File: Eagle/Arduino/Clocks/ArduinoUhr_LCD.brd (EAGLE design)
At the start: 100 x 80 mm, 27 parts, among them IC1 UA748P

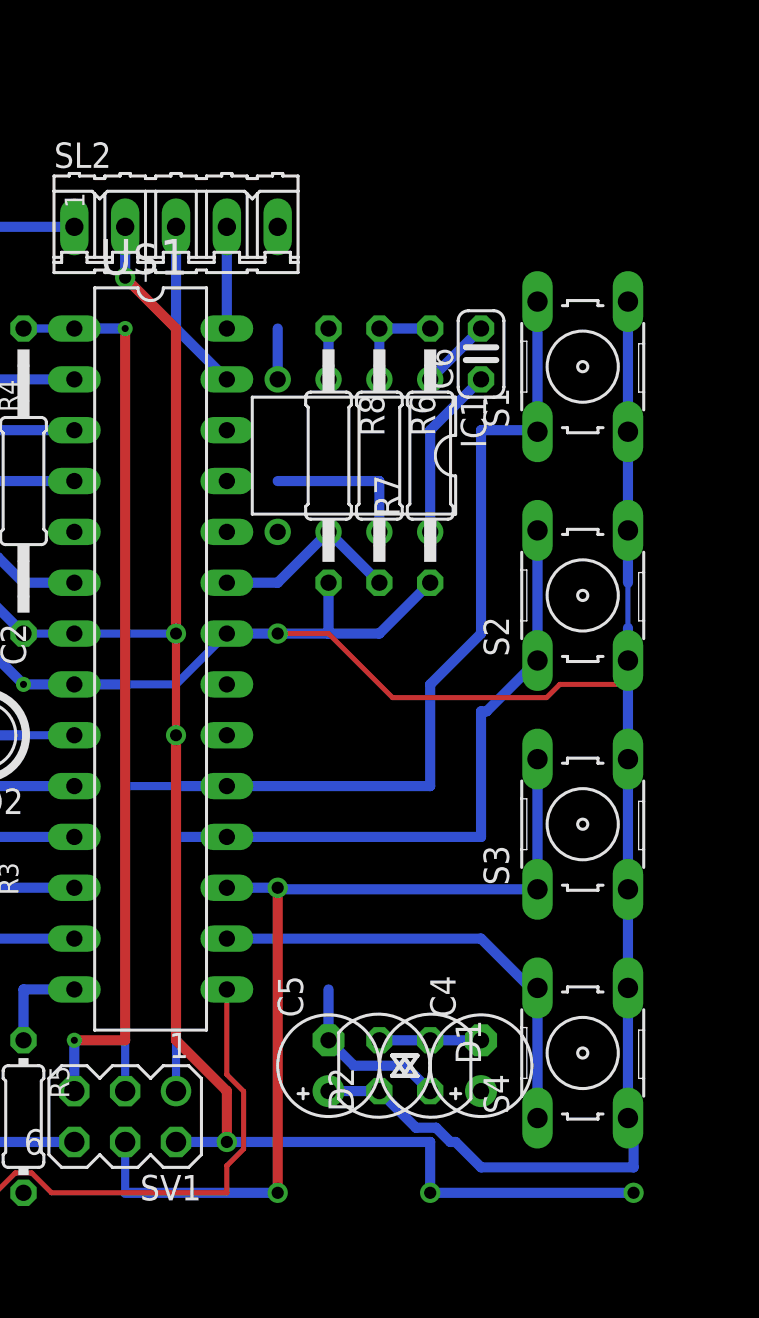
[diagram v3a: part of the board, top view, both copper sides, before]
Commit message: changed schematics - Measurement of current
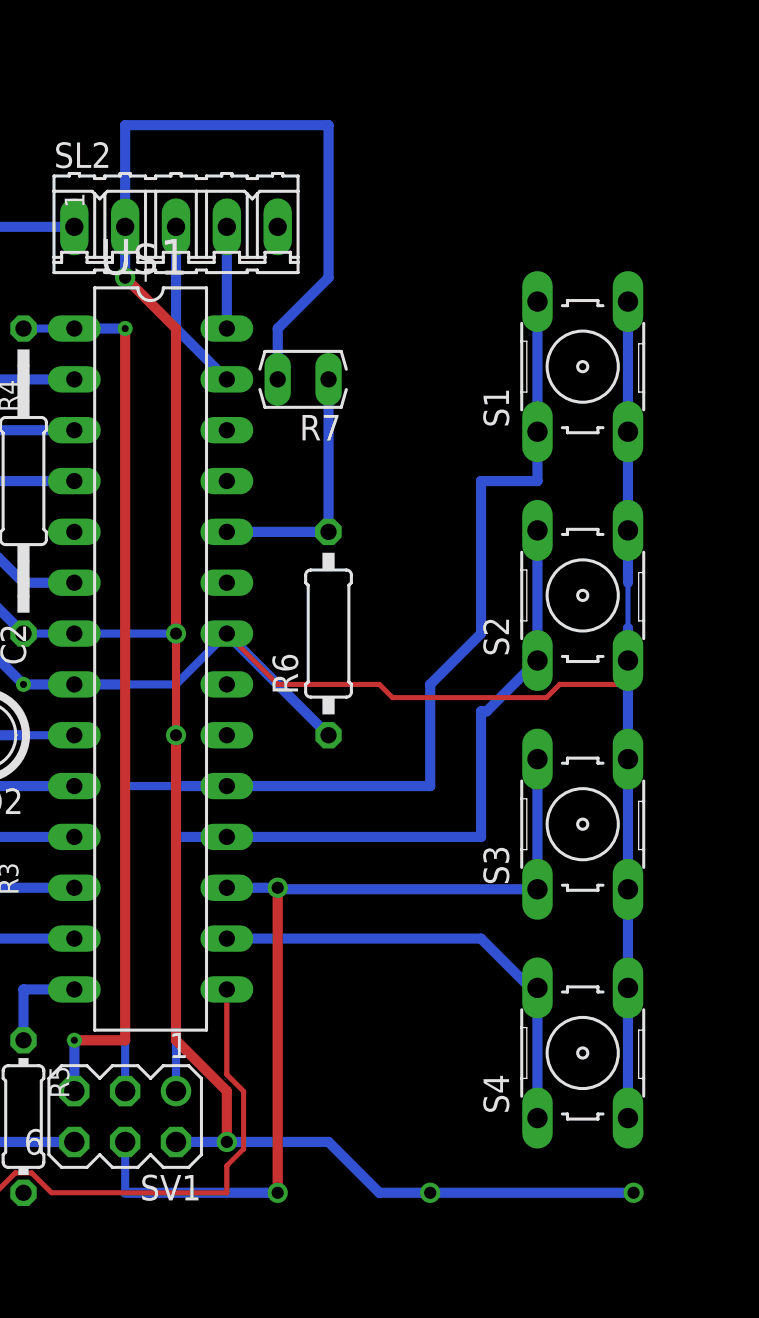
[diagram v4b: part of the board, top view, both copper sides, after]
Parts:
- removed C4, C5: (no value), rcl:E2,5-5
- removed C6: (no value), rcl:C025-024X044
- removed D1, D2: BB112, diode:SOT54H
- removed IC1: UA748P, linear:DIL08
- removed R8: R62, rcl:0207/12
- R6: value 22k -> 150; device rcl:0207/12 -> resistor:0207/10
- R7: value 2k2 -> (none); device rcl:0207/12 -> ptc-ntc:N640
- moved R6 9.25 mm to (55.9, 35.6), turned to 90 degrees
- moved R7 7.41 mm to (54.6, 48.3), turned to 180 degrees
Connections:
- removed net COMP: C6.1, IC1.8
- removed net N$1: C4.-, D1.C, D2.A
- removed net N$4: C6.2, IC1.1
- removed net N$5: IC1.2, R6.1, R7.2
- removed net N2: IC1.5
- removed net OUT_GND: IC1.3, R8.1
- removed net VDD: C5.-, D1.A, IC1.4
- net A0[CURRENT]: no longer IC1.6, R6.2
- net A1[TEMPERATURE]: now also R6.2, R7.1
- net D3: no longer C4.+
- net GND: now also R6.1; no longer C5.+, D2.C, R7.1, R8.2
- net VCC: now also R7.2; no longer IC1.7
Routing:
- net GND: track 218.7 -> 195.6 mm, vias 6 -> 5
- net VCC: track 122.5 -> 142.4 mm
- net A1[TEMPERATURE]: track 0.00 -> 12.7 mm
- net VDD: track 11.2 -> 0.00 mm
- net A0[CURRENT]: track 9.72 -> 0.00 mm
- net COMP: track 8.67 -> 0.00 mm
- net N$5: track 5.08 -> 0.00 mm
- net N$1: track 5.08 -> 0.00 mm
- net N$4: track 3.59 -> 0.00 mm
- net OUT_GND: track 2.54 -> 0.00 mm

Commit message: implemented gitview delete file - imroved eagle circiut for clock with measurement of current
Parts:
- added C4, C5: (no value), rcl:E2-5
- added D1, D2: 1N4148DO35-7, diode:DO35-7
- added IC1: LM324N, linear:DIL14
- added LSP1, LSP2: LSP10, solpad:LSP10
- added R10: 4k7, rcl:0204/7
- added R11: 100, rcl:0204/7
- added R12: 0.56, rcl:P0613/15
- added R13, R14, R9: 22k, rcl:0204/7
- added SL4, SL5: (no value), con-amp-quick:05P
- R6: value 150 -> 10k
- moved S1 25.4 mm to (94.0, 48.9)
- moved S2 25.4 mm to (94.0, 37.5)
- moved S3 25.4 mm to (94.0, 26.0)
- moved S4 25.4 mm to (94.0, 14.6)
- moved C1 17.8 mm to (15.2, 34.3)
- moved C2 17.8 mm to (20.3, 34.3)
- moved C3 17.8 mm to (17.8, 15.2)
- moved Q2 17.8 mm to (17.8, 30.5)
- moved R1 17.8 mm to (22.9, 43.2)
- moved R2 17.8 mm to (15.2, 16.5)
- moved R3 17.8 mm to (20.3, 21.6)
- moved R4 17.8 mm to (20.3, 45.7)
- moved R5 17.8 mm to (22.9, 11.4)
- moved R6 17.8 mm to (38.1, 35.6), turned to 270 degrees
- moved SL1 17.8 mm to (10.2, 21.6)
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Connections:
- net N$3 renamed TONE
- removed net A3: U$1.26
- new net A3_VOLTAGE: R13.2, R14.1, U$1.26
- new net N$1: IC1.6, R10.1, R9.2
- new net N$4: C4.-, D1.C, D2.A
- new net N$6: IC1.5, R11.1
- new net N$8: R11.2, R12.2
- new net SW1: S4.1, S4.2, SL5.4
- new net SW2: S3.1, S3.2, SL5.3
- new net SW3: S2.1, S2.2, SL5.2
- new net SW4: S1.1, S1.2, SL5.1
- new net SW_GND: S1.3, S1.4, S2.3, S2.4, S3.3, S3.4, S4.3, S4.4, SL5.5
- new net V+: IC1.4, LSP1.MP
- new net V-: C5.-, D1.A, IC1.11
- net A0[CURRENT]: now also IC1.7, R9.1
- net A1[TEMPERATURE]: now also R6.1, R7.2; no longer R6.2, R7.1
- net D3: now also C4.+
- net DIO10(PWM)[SW1]: now also SL4.2; no longer S4.1, S4.2
- net DIO11(PWM)MOSI[SW2]: now also SL4.3; no longer S3.1, S3.2
- net DIO12/MISO[SW3]: now also SL4.4; no longer S2.1, S2.2
- net GND: now also C5.+, D2.C, R10.2, R12.1, R14.2, R7.1, SL4.1; no longer R6.1, S1.3, S1.4, S2.3, S2.4, S3.3, S3.4, S4.3, S4.4
- net SCK[SW4]: now also SL4.5; no longer S1.1, S1.2
- net VCC: now also LSP2.MP, R13.1, R6.2; no longer R7.2
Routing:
- net SW_GND: track 0.00 -> 67.6 mm, vias 0 -> 1
- net DIO9(PWM)[LED]: track 58.2 -> 0.00 mm
- net V-: track 0.00 -> 51.3 mm
- net N$8: track 0.00 -> 32.6 mm
- net SW4: track 0.00 -> 29.6 mm
- net SCK[SW4]: track 58.6 -> 30.5 mm
- net A0[CURRENT]: track 0.00 -> 27.5 mm
- net DIO12/MISO[SW3]: track 44.6 -> 25.4 mm
- net SW3: track 0.00 -> 18.6 mm
- net GND: track 195.6 -> 179.8 mm
- net SW1: track 0.00 -> 15.5 mm
- net N$1: track 0.00 -> 15.2 mm
- net DIO10(PWM)[SW1]: track 23.0 -> 10.2 mm
- net DIO11(PWM)MOSI[SW2]: track 47.6 -> 35.7 mm
- net SW2: track 0.00 -> 11.8 mm
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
